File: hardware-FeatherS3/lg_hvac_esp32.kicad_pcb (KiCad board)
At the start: 4 copper layers, 22.9 x 50.8 mm, 20 parts, among them J1 JST_XH_S3B-XH-A-1_01x03, J2 Conn_01x16, J3 Conn_01x12, U1 TPS82130, U2 TJA1027

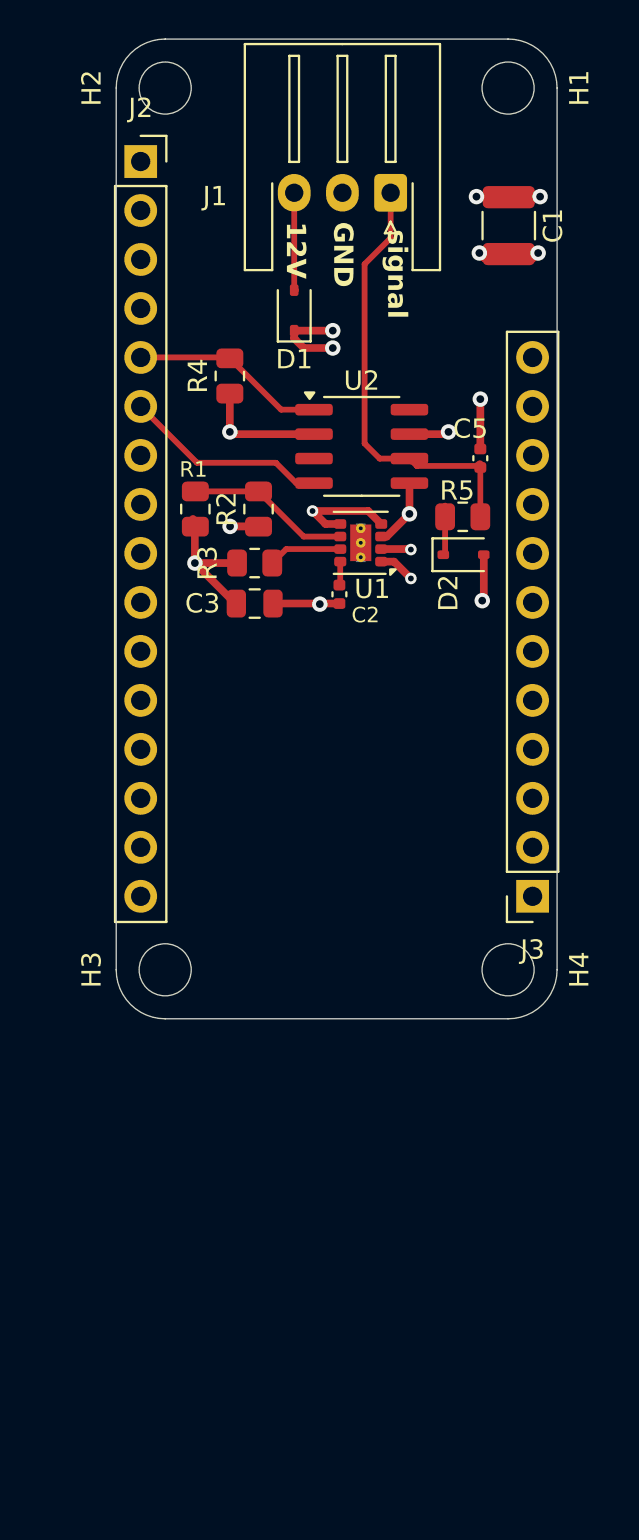
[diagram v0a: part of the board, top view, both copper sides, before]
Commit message: Extend board 25mm past headers, add bottom-side pin labels
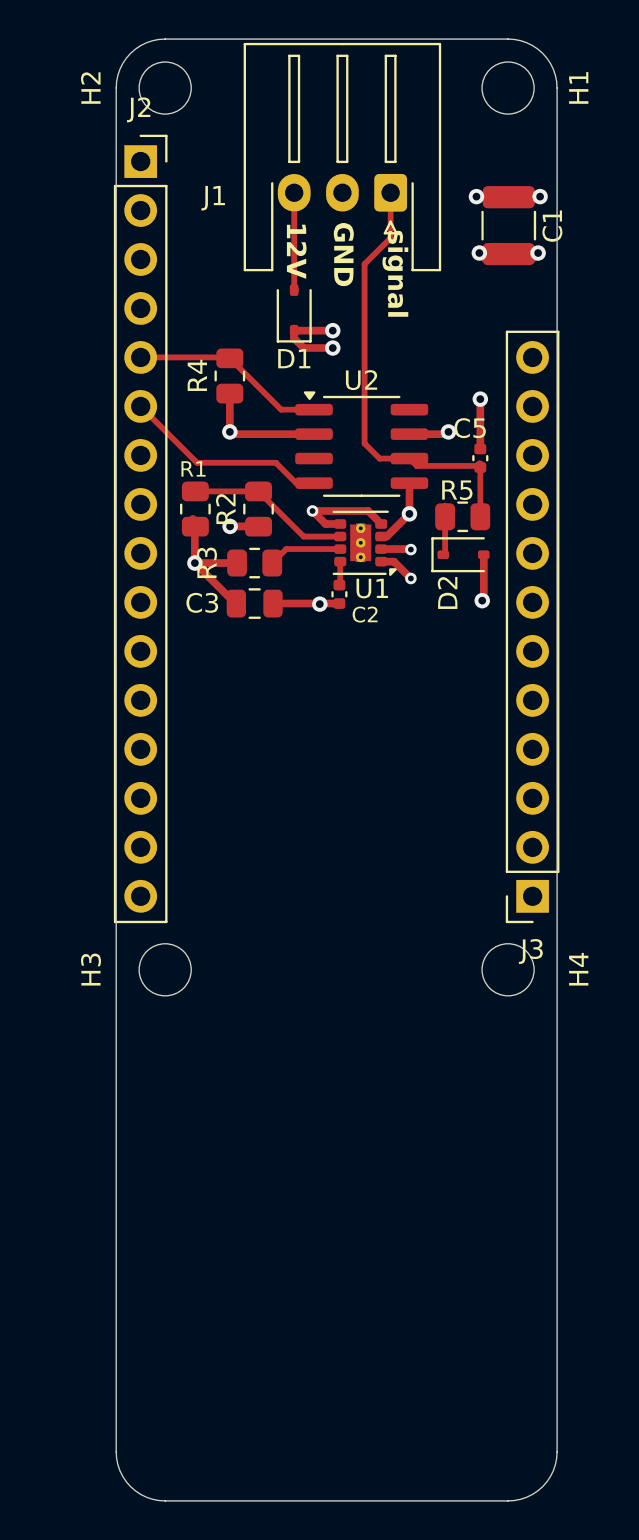
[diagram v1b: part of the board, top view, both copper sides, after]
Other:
- board size 22.9 x 50.8 mm -> 22.9 x 75.8 mm
- board text added: "0"
- board text added: "1"
- board text added: "10"
- board text added: "11"
- board text added: "12"
- board text added: "14"
- board text added: "3"
- board text added: "33"
- board text added: "38"
- board text added: "5"
- board text added: "5V"
- board text added: "6"
- board text added: "7"
- board text added: "BAT"
- board text added: "En"
- board text added: "MI"
- board text added: "MO"
- board text added: "RST"
- board text added: "RX"
- board text added: "SCK"
- board text added: "SCL"
- board text added: "SDA"
- board text added: "TX"
